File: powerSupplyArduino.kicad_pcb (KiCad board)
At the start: 2 copper layers, 61 parts, among them J1 Conn_01x04, J2 Main connector, J3 Display, J4 Termo_sens, J5 ISP, J6 Encoder, U1 LM324, U2 TL494, U3 ATmega8A-AU

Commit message: first try to routing
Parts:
- C15, C17, R16, R17, R19, R2, R20, RV1, RV2, RV3, RV4: moved to B.Cu
- moved J2 77.4 mm to (186.5, 70.0)
- moved R19 63.6 mm to (104.6, 91.0)
- moved C2 63.0 mm to (164.8, 63.7)
- moved C18 61.4 mm to (102.7, 62.0), turned to 90 degrees
- moved R27 55.4 mm to (180.9, 69.9)
- moved J5 53.4 mm to (95.0, 54.9)
- moved C10 52.7 mm to (114.4, 70.0), turned to 270 degrees
- moved R8 48.6 mm to (110.5, 62.4), turned to 270 degrees
- moved R26 45.7 mm to (124.3, 69.7), turned to 90 degrees
- moved C16 44.8 mm to (119.0, 69.8), turned to 90 degrees
- moved RV3 44.4 mm to (109.4, 55.8)
- moved R7 42.8 mm to (179.7, 80.5), turned to 180 degrees
- moved RV1 42.0 mm to (121.8, 55.7)
- moved J1 41.7 mm to (166.4, 55.0), turned to 270 degrees
- moved R4 40.5 mm to (179.6, 76.8)
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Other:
- board outline added: 98 x 56.9 mm
- net class Default: trace_width 0.25 -> 0.5; via_dia 0.8 -> 1.3; via_drill 0.4 -> 0.7

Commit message: change position
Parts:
- R18: moved to B.Cu
- moved R18 25.3 mm to (112.2, 95.4), turned to 180 degrees
- moved C12 22.0 mm to (145.0, 69.0), turned to 90 degrees
- moved R17 18.9 mm to (148.8, 95.6)
- moved C15 17.8 mm to (140.4, 95.5)
- moved R16 13.9 mm to (130.9, 95.6)
- moved R28 11.8 mm to (144.4, 75.4)
- moved R14 11.5 mm to (130.9, 74.7)
- moved R2 10.7 mm to (121.9, 95.2)
- moved C1 9.24 mm to (131.1, 71.4)
- moved C22 8.80 mm to (180.5, 97.3)
- moved C19 7.57 mm to (146.8, 95.7), turned to 180 degrees
- moved C5 5.98 mm to (171.8, 96.8), turned to 0 degrees
- moved R29 5.42 mm to (157.1, 102.1)
- moved R5 5.37 mm to (160.5, 71.4), turned to 0 degrees
- moved R23 4.74 mm to (169.0, 71.4)
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
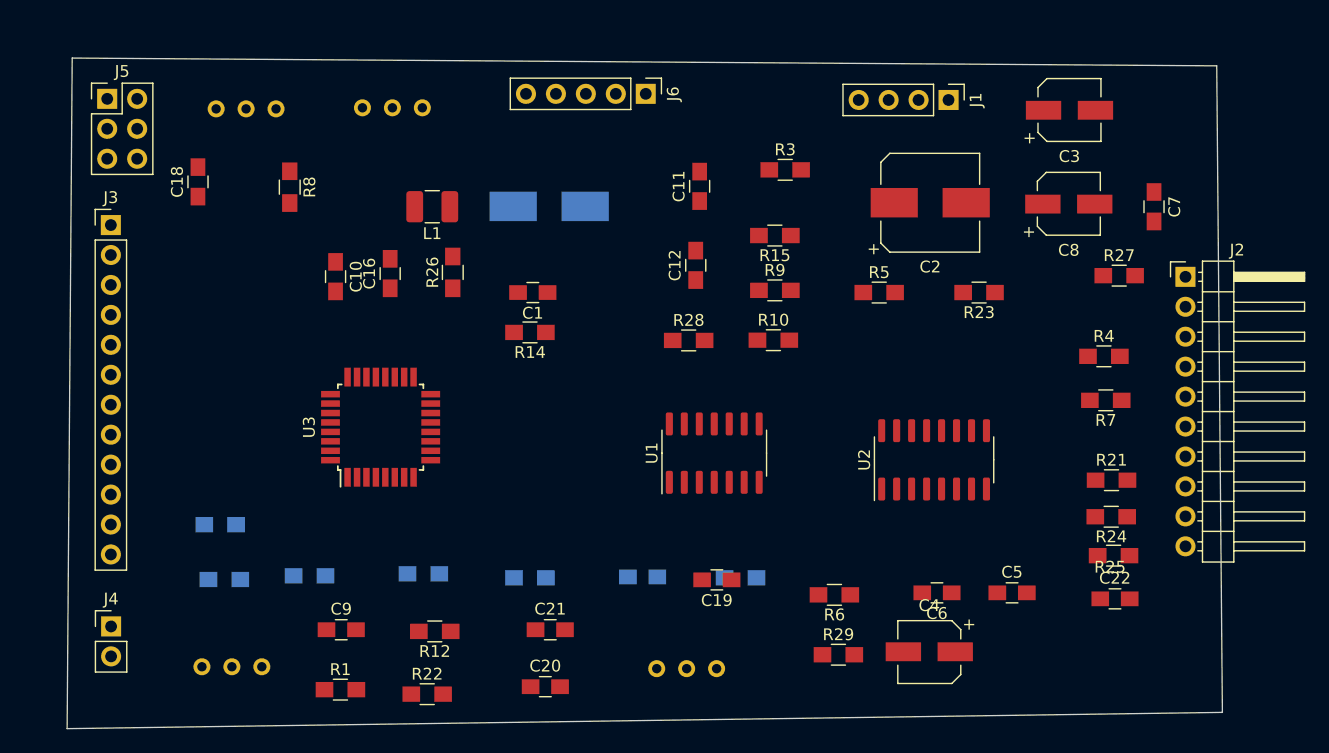
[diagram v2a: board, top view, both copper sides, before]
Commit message: charnge positions. start autorouting
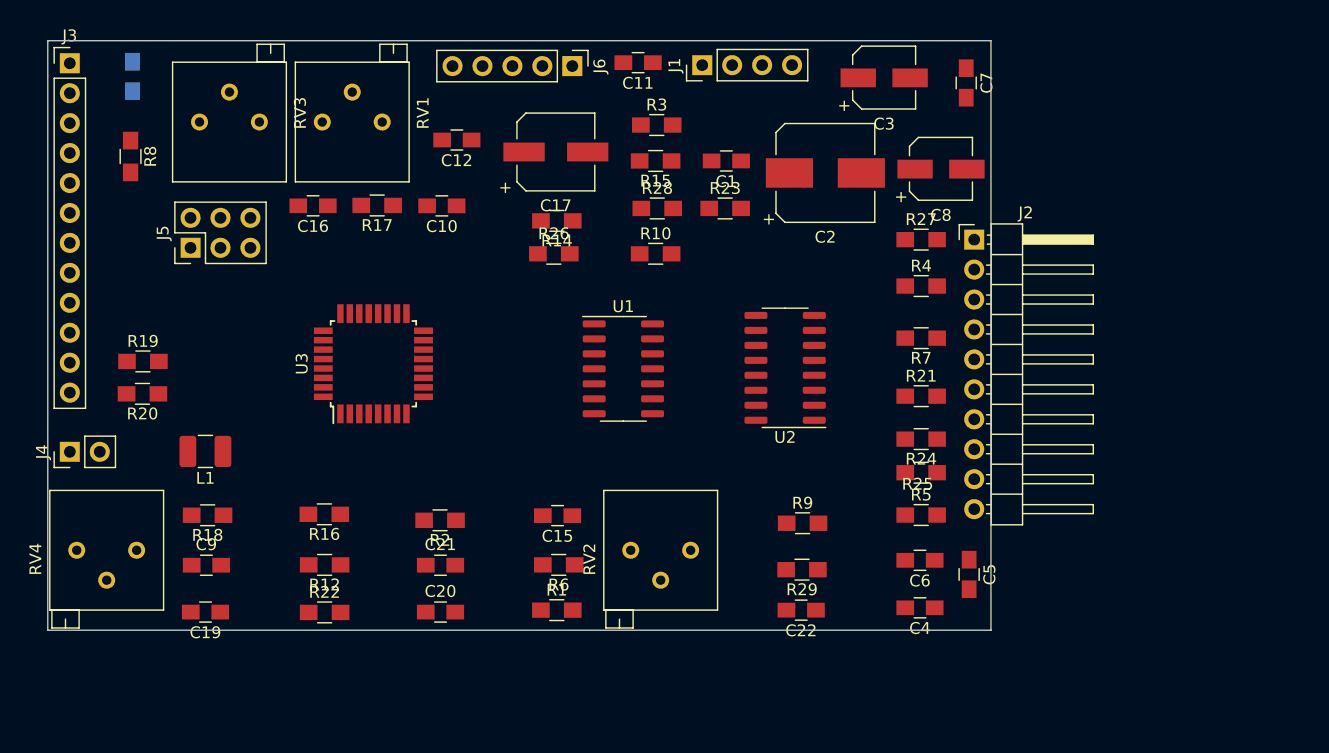
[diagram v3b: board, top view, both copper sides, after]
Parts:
- C15, R16, R17, R18, R19, R2, R20: moved to F.Cu
- C17: footprint Capacitors_SMD:CP_Elec_8x6.5 -> Capacitors_SMD:CP_Elec_6.3x5.3; moved to F.Cu
- C18: moved to B.Cu
- C4: footprint Capacitors_SMD:CP_Elec_5x5.3 -> Capacitors_SMD:C_0805_HandSoldering
- C5: value 10nF -> 33nF
- C6: value 10nF -> 150nF
- J1: value Conn_01x04 -> supply_shunt
- RV1, RV2, RV3, RV4: footprint Potentiometers:Potentiometer_Trimmer_Bourns_3296W -> Potentiometers:Potentiometer_Trimmer_Bourns_3299P; moved to F.Cu
- moved R17 44.1 mm to (117.9, 64.0)
- moved C19 43.5 mm to (103.4, 98.5)
- moved L1 28.3 mm to (103.4, 84.8)
- moved C22 26.6 mm to (153.9, 98.3), turned to 180 degrees
- moved R6 23.5 mm to (133.3, 94.5)
- moved C12 22.9 mm to (124.7, 58.4), turned to 180 degrees
- moved R23 22.7 mm to (147.5, 64.2), turned to 0 degrees
- moved J1 21.1 mm to (145.5, 52.1), turned to 90 degrees
- moved R9 19.9 mm to (154.0, 90.9)
- moved C1 19.8 mm to (147.6, 60.2)
- moved R1 19.6 mm to (133.2, 98.3)
- moved R5 19.2 mm to (164.1, 90.2)
- moved C7 19.1 mm to (167.9, 53.6)
- moved R16 18.3 mm to (113.5, 90.2)
- moved J2 18.2 mm to (168.6, 66.9)
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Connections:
- R4 pad 1: Net-(C4-Pad1) -> Net-(C4-Pad2)
- R4 pad 2: Net-(C4-Pad2) -> Net-(C4-Pad1)
- R7 pad 2: Net-(C4-Pad2) -> Net-(C4-Pad1)
- U2 pad 13: Net-(C4-Pad1) -> Net-(C4-Pad2)
- U2 pad 14: Net-(C4-Pad1) -> Net-(C4-Pad2)
- U2 pad 4: Net-(C4-Pad2) -> Net-(C4-Pad1)
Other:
- board size 98 x 56.9 mm -> 80 x 50 mm

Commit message: charnge positions. start autorouting again
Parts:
- C1, C10, C12, C16, C4, C5, R17, R21, R23, R25, R3, R4, R5, R7, R9: moved to B.Cu
- moved C9 71.3 mm to (174.7, 94.4), turned to 180 degrees
- moved R12 61.4 mm to (174.8, 91.0), turned to 0 degrees
- moved R22 61.3 mm to (174.8, 97.9), turned to 180 degrees
- moved R2 52.2 mm to (174.8, 82.7), turned to 0 degrees
- moved R1 46.0 mm to (174.8, 78.8)
- moved R25 44.7 mm to (119.8, 92.7), turned to 90 degrees
- moved R24 42.0 mm to (123.0, 92.6), turned to 90 degrees
- moved C15 41.7 mm to (174.7, 86.3), turned to 0 degrees
- moved C4 41.2 mm to (135.2, 68.6), turned to 0 degrees
- moved R21 40.0 mm to (126.1, 92.7), turned to 270 degrees
- moved J2 39.8 mm to (143.0, 97.4), turned to 270 degrees
- moved RV2 39.3 mm to (173.2, 73.1), turned to 180 degrees
- moved R7 35.6 mm to (133.1, 92.7), turned to 90 degrees
- moved R27 35.0 mm to (149.0, 98.5), turned to 180 degrees
- moved C5 34.3 mm to (146.8, 68.4), turned to 0 degrees
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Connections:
- J4 pad 2: +5V -> GND
- R20 pad 2: GND -> +5V
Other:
- board size 80 x 50 mm -> 90 x 50 mm

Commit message: charnge positions. start autorouting again 2
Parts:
- moved R20 7.60 mm to (99.1, 87.3)
- moved R19 3.80 mm to (96.1, 77.3)
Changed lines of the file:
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@@
   )
   (module Resistors_SMD:R_0805_HandSoldering (layer F.Cu)
-    (at 99.87 79.73)
+    (at 99.09 87.29)
     (descr "Resistor SMD 0805, hand soldering")
     (tags "resistor 0805")
@@
   )
   (module Resistors_SMD:R_0805_HandSoldering (layer F.Cu)
-    (at 99.9 77.12)
+    (at 96.1 77.26)
     (descr "Resistor SMD 0805, hand soldering")
     (tags "resistor 0805")

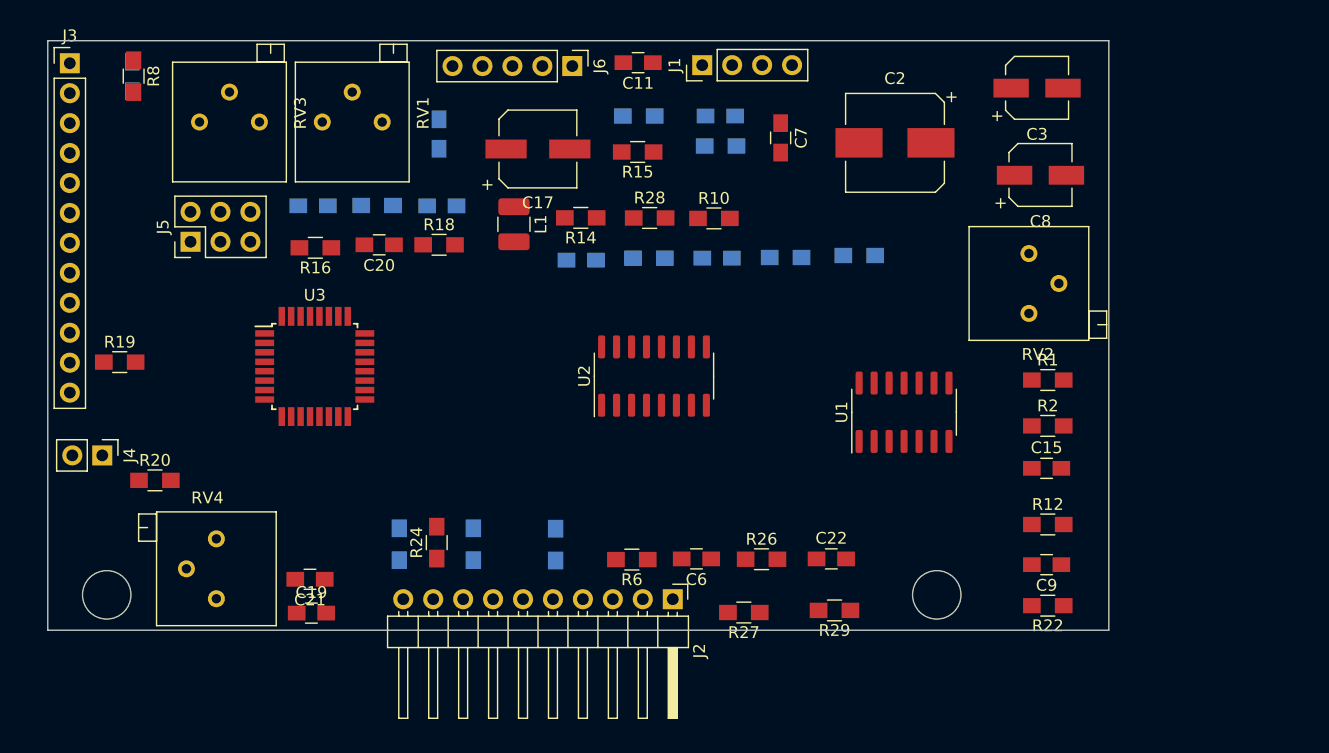
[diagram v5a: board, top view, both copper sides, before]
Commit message: width chnged to .6 mm
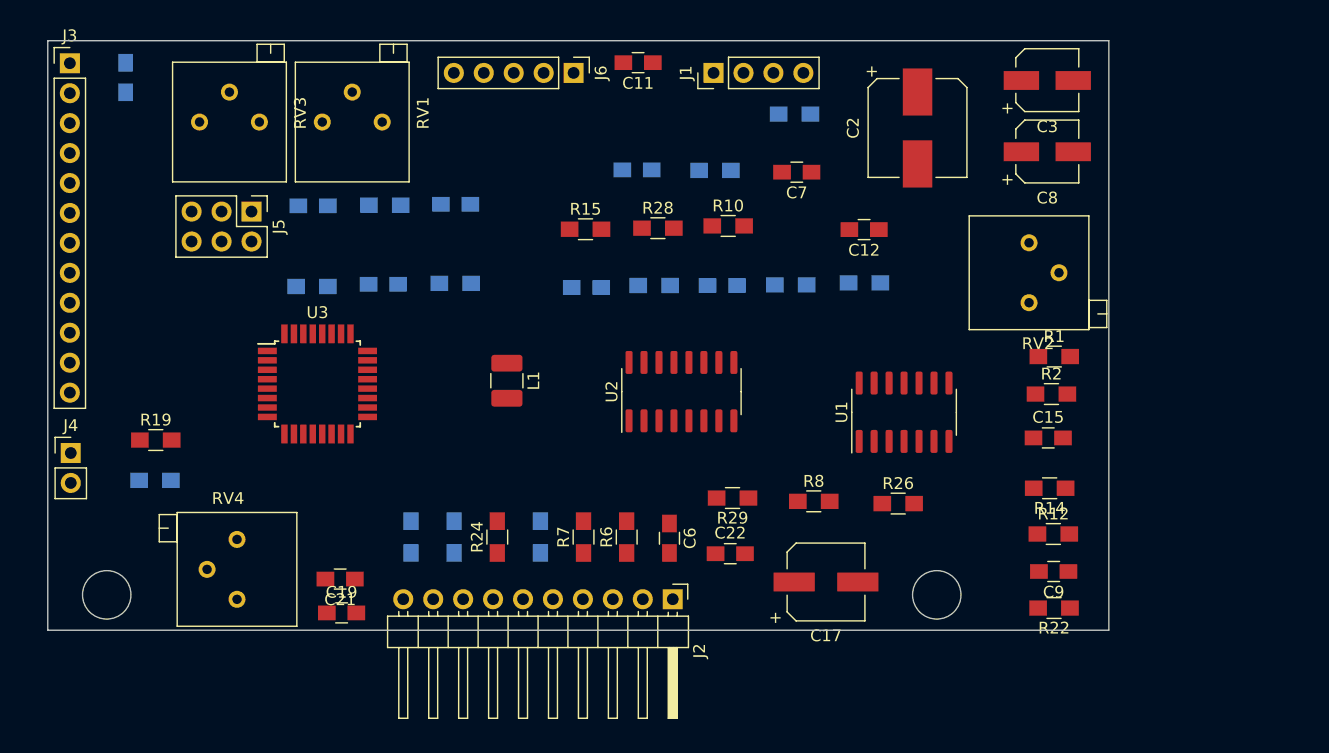
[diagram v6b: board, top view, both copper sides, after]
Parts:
- C12, R7: moved to F.Cu
- C20, R16, R18, R20, R27: moved to B.Cu
- moved R8 68.0 mm to (155.0, 89.1), turned to 0 degrees
- moved R14 45.9 mm to (175.0, 88.0)
- moved C17 44.1 mm to (156.0, 95.9)
- moved C12 37.0 mm to (159.2, 66.0), turned to 180 degrees
- moved R27 28.9 mm to (120.8, 92.1), turned to 270 degrees
- moved L1 13.3 mm to (128.9, 78.8)
- moved R3 13.2 mm to (153.3, 56.2)
- moved R29 12.9 mm to (148.1, 88.8)
- moved R26 12.5 mm to (162.1, 89.3)
- moved C22 8.58 mm to (147.9, 93.5)
- moved C1 8.42 mm to (140.0, 61.0)
- moved R15 7.91 mm to (135.6, 66.0), turned to 0 degrees
- moved R19 7.28 mm to (99.2, 83.9)
- moved J5 5.77 mm to (107.3, 64.5), turned to 270 degrees
- moved R21 5.72 mm to (131.8, 92.1)
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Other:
- net class Default: trace_width 0.5 -> 0.6

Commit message: routing complite
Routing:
- net GND: track 0.00 -> 415.0 mm
- net +5V: track 0.00 -> 274.9 mm, vias 0 -> 2
- net +15V: track 0.00 -> 129.6 mm, vias 0 -> 3
- net Supply-: track 0.00 -> 120.7 mm
- net Encoder_S: track 0.00 -> 109.9 mm, vias 0 -> 1
- net Q3Base: track 0.00 -> 109.1 mm
- net Net-(R12-Pad1): track 0.00 -> 107.0 mm
- net Net-(R10-Pad1): track 0.00 -> 85.8 mm, vias 0 -> 1
- net Encoder_A: track 0.00 -> 85.2 mm, vias 0 -> 1
- net Net-(C20-Pad1): track 0.00 -> 81.6 mm, vias 0 -> 1
- net ISP_VCC: track 0.00 -> 77.3 mm, vias 0 -> 1
- net Net-(C7-Pad2): track 0.00 -> 71.5 mm, vias 0 -> 2
- net Q4Base: track 0.00 -> 71.1 mm, vias 0 -> 1
- net Encoder_B: track 0.00 -> 71.1 mm, vias 0 -> 1
- net Net-(R8-Pad1): track 0.00 -> 69.2 mm, vias 0 -> 1
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
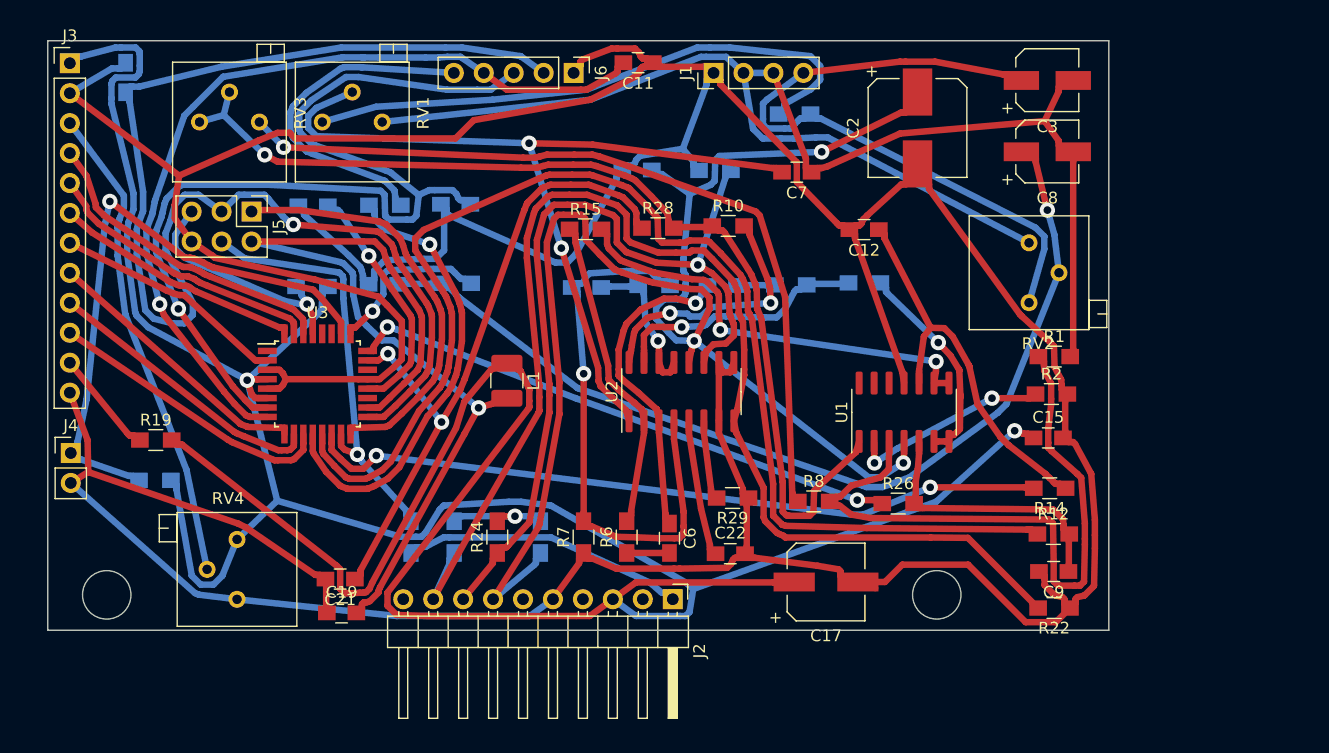
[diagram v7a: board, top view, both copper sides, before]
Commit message: add zones
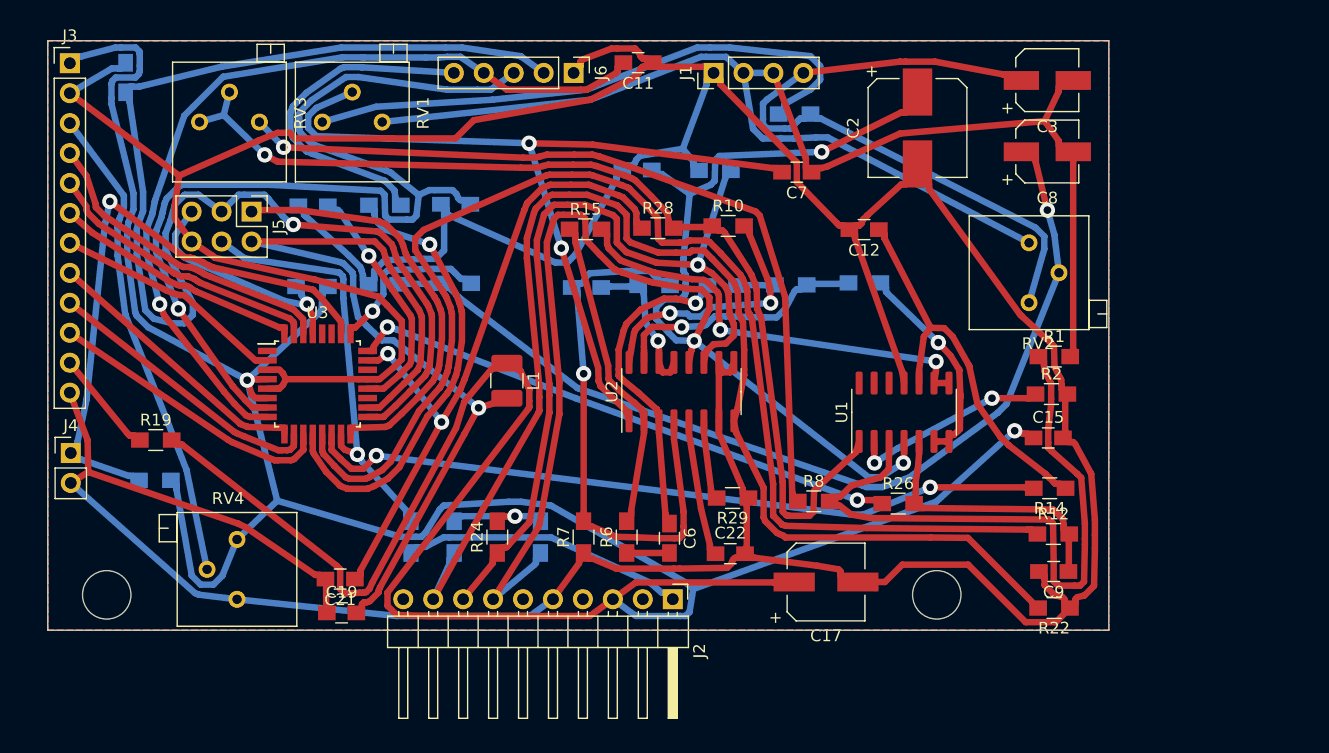
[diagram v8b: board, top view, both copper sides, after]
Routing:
- added copper zone on B.Cu, net GND
- added copper zone on F.Cu, net GND
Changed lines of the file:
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@@
+    )
+  )
+  (zone (net 2) (net_name GND) (layer F.Cu) (hatch edge 0.508)
+    (connect_pads (clearance 0))
+    (min_thickness 0.254)
+    (fill yes (arc_segments 32) (thermal_gap 0.508) (thermal_bridge_width 0.508))
+    (polygon
+      (pts
+        (xy 90 99.99) (xy 90 50) (xy 180 50) (xy 180 100)
+      )
+    )
+  )
+  (zone (net 2) (net_name GND) (layer F.Cu) (hatch edge 0.508)
+    (connect_pads (clearance 0))
+    (min_thickness 0.254)
+    (fill yes (arc_segments 32) (thermal_gap 0.508) (thermal_bridge_width 0.508))
+    (polygon
+      (pts
+        (xy 180 100) (xy 180 50) (xy 90 50) (xy 90 99.98)
+      )
+    )
+  )
+  (zone (net 2) (net_name GND) (layer B.Cu) (hatch edge 0.508)
+    (connect_pads (clearance 0))
+    (min_thickness 0.254)
+    (fill yes (arc_segments 32) (thermal_gap 0.508) (thermal_bridge_width 0.508))
+    (polygon
+      (pts
+        (xy 180.01 99.99) (xy 180 50) (xy 90 50) (xy 90.01 99.99)
+      )
     )
   )
